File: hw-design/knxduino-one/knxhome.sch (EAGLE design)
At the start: 47 parts, among them IC1 LDL1117S33, IC2 STM32G071CBT6, IC3 BD9G101, P1 B10B-PH-K, P2 B10B-PH-K, P3 B6B-PH-K, U1 OSCILLATOR5X3-PIN1-INDICATED

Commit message: HW files cleanup and image previews
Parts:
- removed C10*: 10p, rcl:C-EUC0805
- removed C12, C13*: 10n, rcl:C-EUC0805
- removed C13: 4u7, rcl:C-EUC0805
- removed C16: 270n, rcl:C-EUC0805
- removed C17: 15nF, rcl:C-EUC0805
- removed D100: MBRS1100, diode:MBRA340T3
- removed D2*: 3V3, diode:ZENER-DIODESOT23
- removed IC2: STM32G071CBT6, stm32g0:STM32G071CBT6
- removed IC3: BD9G101, Stefan_selfbus:BD9G101GBD9G101G-SOT23-6
- removed L1: FERRITE BEAD, inductor-neosid:SM-B5
- removed L2: 6.8µH, Stefan_selfbus:IND_FASTRON_1616FPS
- removed R25: 2k4, rcl:R-EU_R0805
- removed R26: 680R, rcl:R-EU_R0805
- added +5V: (no value), SparkFun-Connectors:CONN_01PTH_LONGPAD
- added C2', C3': *, rcl:C-EUC1210
- added C4: 100uF 50V, rcl:CPOL-EUE3.5-8
- added C4': (no value), resistor:CPOL-EU153CLV-0810
- added C7: 1u, rcl:C-EUC0805
- added D2: SMAJ15CA, diode:SMAJ40AC
- added I2CB_U: (no value), jumper:SJ2W
- added IC4: STM32G071KBT6, stm32g0:STM32G071KBT6
- added LED2, RX, TX: *, led:LEDCHIPLED_1206
- added R1: 510R*, rcl:R-EU_R0805
- added R11, R12: 10k, rcl:R-EU_R0805
- added RX., TX.: (no value), pinhead:PINHD-1X1
- added U2: VXO7803-500, VXO7803-500:VXO7803-500
- C10: value 1u -> 10p*
- C2: value 4.7µF/50V -> 10µF/50V; device rcl:C-EUC0805 -> rcl:C-EUC1210
- C3: value 100n -> 22µ/10V; device rcl:C-EUC0805 -> rcl:C-EUC1210
- C8: value 22µ/10V -> 4u7
- C9: value 100uF 50V -> 100n; device rcl:CPOL-EUE3.5-8 -> rcl:C-EUC0805
- D11: device diode:DIODE-D0805 -> diode:DIODE-SOD123
- D4: value 3V3 -> 3V3*
- D6: device zetex:DSOD323 -> diode:DIODE-SOD123
- LED1: device led:LEDCHIP-LED0805 -> led:LEDCHIPLED_1206
- R8: value 33k -> 510R*
- R9: value 1k -> 510R*
- renumbered D4* to D4
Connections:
- removed net ADJ: C16.1, IC3.ADJ, R25.1, R26.2
- removed net IOB_PB8: IC2.PB8, P3.5
- removed net IO_PB0: IC2.PB0, P2.7
- removed net IO_PB12: IC2.PB12, P2.1
- removed net IO_PB13: IC2.PB13, P2.2
- removed net KNX_DC_AN: C13*.1, D2*.C, IC2.PA4, R8.1, R9.2
- removed net LED2: IC2.PD2, R10.2
- removed net LX: C17.1, D100.C, IC3.OUT, L2.1
- removed net N$19: C17.2, IC3.BST
- removed net N$5: IC2.PA0, IC2.PA2
- removed net VDDA: C3.1, IC2.VREF+, L1.2
- new net I2C_PUP1: I2CB_U.2, R11.2, R12.2
- new net IOB_AUX: IC4.PB6, P3.3
- new net IO_PA4: IC4.PA4, P2.7
- new net IO_PA8: IC4.PA8, P2.1
- new net IO_PB3: IC4.PB3, LED2.A, P2.3
- new net IO_PB4: IC4.PB4, P2.4
- new net IO_PB5: IC4.PB5, P2.5
- new net IO_PB9: IC4.PB9, P2.6
- new net IO_PC6: IC4.PC6, P2.2
- new net KNX_RX: IC4.PA0, IC4.PA2, RX..1, RX.C
- new net N$2: LED1.C, R10.2
- new net N$3: R1.2, TX.C
- new net N$6: LED2.C, R9.2
- net +3V3: now also C8.1, I2CB_U.3, IC4.VDD, R8.2; no longer C13.1, IC2.VBAT, IC2.VDD, L1.1
- net BTN: now also IC4.PC15-OSC32_OUT; no longer IC2.PD0
- net DRX: now also IC4.PA10; no longer IC2.PA10
- net DTX: now also IC4.PA9; no longer IC2.PA9
- net GND: now also C2'.1, C3'.1, C3.1, C4'.-, C4.-, C7.2, C8.2, D2.A, IC4.VSS, R1.1, R10.1, U2.GND/-VOUT; no longer C10*.2, C13*.2, C13.2, C3.2, C8.1, C9.-, D100.A, D2*.A, IC2.VSS, IC3.GND, R26.1
- net I2CB_SCL: now also IC4.PB8, P3.5, R11.1; no longer IC2.PB6, P3.3
- net I2CB_SDA: now also IC4.PB7, R12.1; no longer IC2.PB7
- net I2C_SCL: now also IC4.PA11; no longer IC2.PB10
- net I2C_SDA: now also IC4.PA12; no longer IC2.PB11
- net IO_AN: now also IC4.PA5; no longer IC2.PA5
- net IO_DE: now also IC4.PB1; no longer IC2.PB1
- net IO_PA6: now also IC4.PA6; no longer IC2.PA6
- net IO_PA7: now also IC4.PA7; no longer IC2.PA7
- net IO_RX: now also IC4.PB0; no longer IC2.PB9
- net IO_TX: now also IC4.PB2; no longer IC2.PB2
- net KNX_DC: now also C2'.2, C4'.+, C4.+, U2.+VIN; no longer C9.+, IC3.EN, IC3.IN, R8.2
- net KNX_RX_AN: now also C10.1, IC4.PA1; no longer C10*.1, IC2.PA1
- net KNX_TX: now also C9.1, IC4.PA3, TX..1, TX.A; no longer C12.1, IC2.PA3
- net LED: now also IC4.PA15; no longer IC2.PD1
- net N$4: now also R8.1, RX.A; no longer LED1.C, R10.1
- net N$8: now also C9.2; no longer C12.2
- net NRST: now also IC4.PF2-NRST; no longer IC2.PF2-NRST
- net OSC: now also IC4.PC14-OSC32_IN; no longer IC2.PF0-OSC_IN
- net SWCLK: now also IC4.PA14-BOOT0; no longer IC2.PA14-BOOT0
- net SWDIO: now also IC4.PA13; no longer IC2.PA13
- net VCC: now also +5V.1, C3'.2, C3.2, C7.1, D2.C, I2CB_U.1, U2.+VOUT/GND; no longer C10.1, C16.2, C8.2, L2.2, R25.2
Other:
- note added: "Either: +5V line supplied Connect external +5V (3rd wire)"
- note added: "Known issues: 0805 diodes are quite expensive (uncommon)! Make PCB bigger in order to better fit into ITALTRONIC KNX BOX. Revise D6 and D11 packages RGB LEDs wont work with 3v3 power supply"
- note added: "Note: PC13, PC14 and PC15 cannot be used as current source"
- note added: "Optional: Debug LEDs"
- note added: "Or: KNX-supplied"
- note removed: "Known issues: Use switch with longer leads (adjust PCB)? no necessary. 0805 diodes are quite expensive (uncommon)! Bigger package for current sensing R! Bigger package for 10u C and 22uF at DCDC! Ferite bead peads are too small Make STCS1 pads longer for hand soldering Bigger radius place for 100uF and/or consider using SMD version Make PCB bigger in order to better fit into ITALTRONIC KNX BOX. C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"
- moved on the sheet: C10, C2, C3, C8, D11, IC1, L3, LED1, R10, R7, R8, R9

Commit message: Schematic more compact
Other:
- note added: "Known issues: Revise D6 and D11 packages"
- note added: "Optional: I2C pullups"
- note added: "Optional: Precise oscillator"
- note added: "Optional: Secondary I2C pullups"
- note removed: "Known issues: 0805 diodes are quite expensive (uncommon)! Make PCB bigger in order to better fit into ITALTRONIC KNX BOX. Revise D6 and D11 packages RGB LEDs wont work with 3v3 power supply"
- moved on the sheet: +5V, C1, C2, C2', C3, C3', C4, C4', C5, C6, C7, C8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

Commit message: Top and bot. board values presets, values adjusted
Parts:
- LED1: value (none) -> RED
- LED2: value * -> BLUE*
- RX: value * -> GREEN*
- TX: value * -> YELLOW*
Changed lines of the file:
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@@
 <part name="L3" library="inductor-neosid" deviceset="SD12" device="BS11_LIEGEND" value="150mH"/>
 <part name="PROG" library="switch-tact" deviceset="DTSM-3" device=""/>
-<part name="LED1" library="led" library_urn="urn:adsk.eagle:library:259" deviceset="LED" device="CHIPLED_1206" package3d_urn="urn:adsk.eagle:package:15823/2"/>
+<part name="LED1" library="led" library_urn="urn:adsk.eagle:library:259" deviceset="LED" device="CHIPLED_1206" package3d_urn="urn:adsk.eagle:package:15823/2" value="RED"/>
 <part name="R10" library="rcl" library_urn="urn:adsk.eagle:library:334" deviceset="R-EU_" device="R0805" package3d_urn="urn:adsk.eagle:package:23553/2" value="510R"/>
 <part name="GND15" library="supply1" deviceset="GND" device=""/>
@@
 <part name="C3'" library="rcl" library_urn="urn:adsk.eagle:library:334" deviceset="C-EU" device="C1210" package3d_urn="urn:adsk.eagle:package:23619/2" value="*"/>
 <part name="GND18" library="supply1" deviceset="GND" device=""/>
-<part name="TX" library="led" library_urn="urn:adsk.eagle:library:259" deviceset="LED" device="CHIPLED_1206" package3d_urn="urn:adsk.eagle:package:15823/2" value="*"/>
+<part name="TX" library="led" library_urn="urn:adsk.eagle:library:259" deviceset="LED" device="CHIPLED_1206" package3d_urn="urn:adsk.eagle:package:15823/2" value="YELLOW*"/>
 <part name="R1" library="rcl" library_urn="urn:adsk.eagle:library:334" deviceset="R-EU_" device="R0805" package3d_urn="urn:adsk.eagle:package:23553/2" value="510R*"/>
 <part name="GND21" library="supply1" deviceset="GND" device=""/>
-<part name="RX" library="led" library_urn="urn:adsk.eagle:library:259" deviceset="LED" device="CHIPLED_1206" package3d_urn="urn:adsk.eagle:package:15823/2" value="*"/>
+<part name="RX" library="led" library_urn="urn:adsk.eagle:library:259" deviceset="LED" device="CHIPLED_1206" package3d_urn="urn:adsk.eagle:package:15823/2" value="GREEN*"/>
 <part name="R8" library="rcl" library_urn="urn:adsk.eagle:library:334" deviceset="R-EU_" device="R0805" package3d_urn="urn:adsk.eagle:package:23553/2" value="510R*"/>
 <part name="+3V4" library="supply1" library_urn="urn:adsk.eagle:library:371" deviceset="+3V3" device=""/>
-<part name="LED2" library="led" library_urn="urn:adsk.eagle:library:259" deviceset="LED" device="CHIPLED_1206" package3d_urn="urn:adsk.eagle:package:15823/2" value="*"/>
+<part name="LED2" library="led" library_urn="urn:adsk.eagle:library:259" deviceset="LED" device="CHIPLED_1206" package3d_urn="urn:adsk.eagle:package:15823/2" value="BLUE*"/>
 <part name="R9" library="rcl" library_urn="urn:adsk.eagle:library:334" deviceset="R-EU_" device="R0805" package3d_urn="urn:adsk.eagle:package:23553/2" value="510R*"/>
 <part name="GND22" library="supply1" deviceset="GND" device=""/>

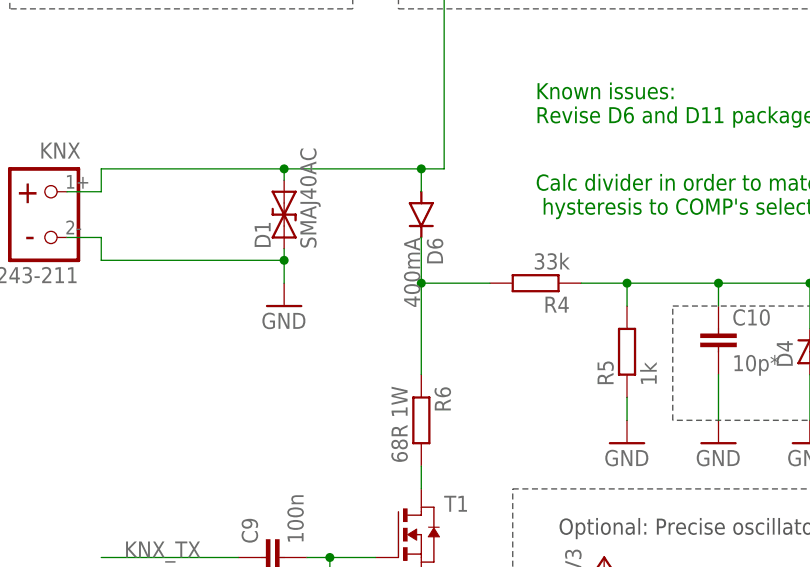
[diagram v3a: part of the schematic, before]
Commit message: Bootloader with diff-support and STM32G0 support
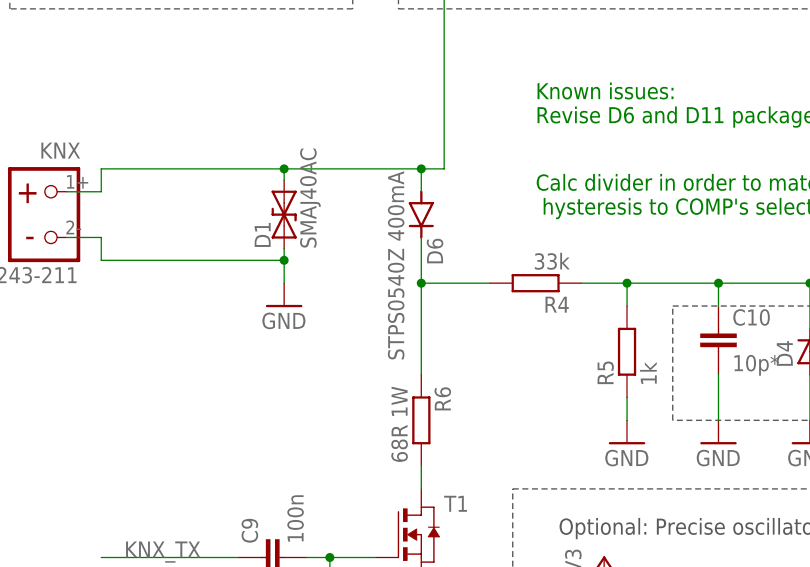
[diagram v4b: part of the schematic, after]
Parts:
- D6: value 400mA -> STPS0540Z 400mA
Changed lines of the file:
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@@
 <part name="R7" library="rcl" library_urn="urn:adsk.eagle:library:334" deviceset="R-EU_" device="R0805" package3d_urn="urn:adsk.eagle:package:23553/2" value="10k"/>
 <part name="GND19" library="supply1" deviceset="GND" device=""/>
-<part name="D6" library="diode" library_urn="urn:adsk.eagle:library:210" deviceset="DIODE-" device="SOD123" package3d_urn="urn:adsk.eagle:package:43420/1" value="400mA"/>
+<part name="D6" library="diode" library_urn="urn:adsk.eagle:library:210" deviceset="DIODE-" device="SOD123" package3d_urn="urn:adsk.eagle:package:43420/1" value="STPS0540Z 400mA"/>
 <part name="D11" library="diode" deviceset="DIODE-" device="SOD123" value="TS4148"/>
 <part name="DBG" library="SparkFun-Connectors" library_urn="urn:adsk.eagle:library:513" deviceset="CONN_07" device="LOCK" package3d_urn="urn:adsk.eagle:package:38132/1"/>
@@
 <instance part="D6" gate="G$1" x="-152.4" y="124.46" smashed="yes" rot="R270">
 <attribute name="NAME" x="-151.765" y="121.92" size="1.778" layer="95" rot="R270"/>
-<attribute name="VALUE" x="-154.305" y="121.92" size="1.778" layer="96" rot="R270"/>
+<attribute name="VALUE" x="-156.083" y="129.286" size="1.778" layer="96" rot="R270"/>
 </instance>
 <instance part="D11" gate="G$1" x="-147.32" y="162.56" smashed="yes">
